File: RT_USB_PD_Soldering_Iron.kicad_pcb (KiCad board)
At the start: 4 copper layers, 75 x 11 mm, 63 parts, among them J1 USB_C_Receptacle_USB2.0, J2 35RASMT4BHNTRX, SW1 SW_Push, SW2 SW_Push, U1 SPX3819M5-L-3-3, U2 BMI270, U3 DRTR5V0U4S-7, U5 STM32G431Kxxx, U6 TPS25982ONRGET, U7 OPA376AIDCKR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

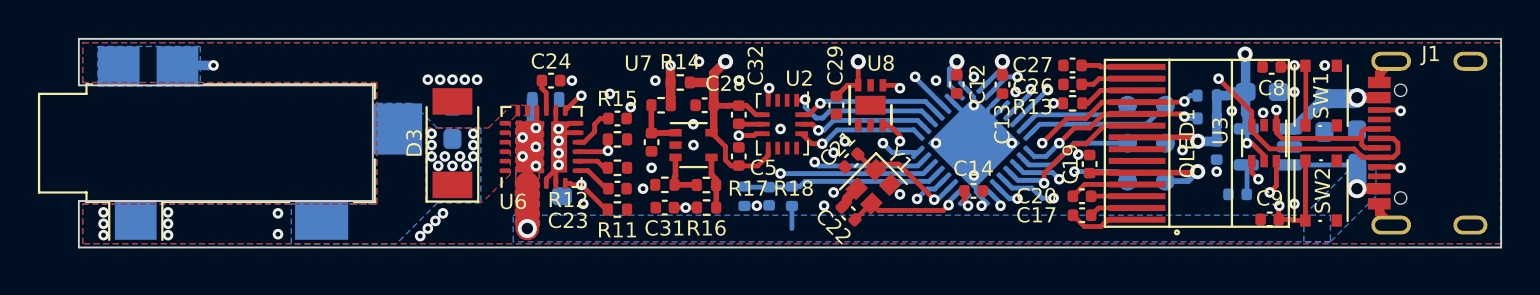
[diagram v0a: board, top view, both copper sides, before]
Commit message: update libs/parts
update 0402 footprints for silkscreen
move volate/tolerance to value
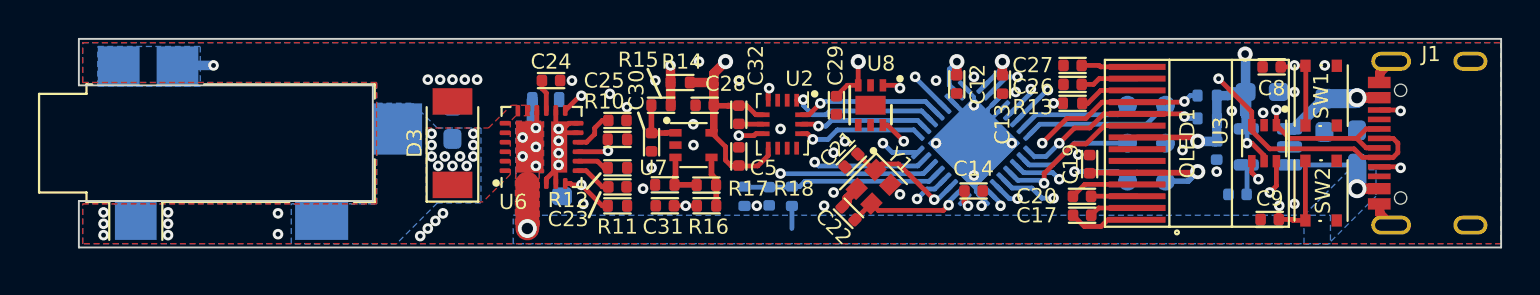
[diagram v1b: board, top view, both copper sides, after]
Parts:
- C1, C15, C16, C2, C33: value 10uF -> 10uF 35v
- C12, C13, C14, C18, C19, C28, C29, C32, C5, C8, C9: value 0.1uF -> 0.1uF 50v; footprint Capacitor_SMD:C_0402_1005Metric -> Basic_SMD:C_0402_1005Metric
- C17, C20, C4: value 1u -> 1u 50v; footprint Capacitor_SMD:C_0402_1005Metric -> Basic_SMD:C_0402_1005Metric
- C21, C22: value 6.8p -> 6.8p 50v; footprint Capacitor_SMD:C_0402_1005Metric -> Basic_SMD:C_0402_1005Metric
- C23, C25, C3, C30, C31: value 10000pF -> 10000pF 50v; footprint Capacitor_SMD:C_0402_1005Metric -> Basic_SMD:C_0402_1005Metric
- C24: value 1200pF -> 1200pF 50v; footprint Capacitor_SMD:C_0402_1005Metric -> Basic_SMD:C_0402_1005Metric
- C26, C27: value 2.2u -> 2.2u 25v; footprint Capacitor_SMD:C_0402_1005Metric -> Basic_SMD:C_0402_1005Metric
- J1: value USB_C_Receptacle_USB2.0 -> USB4105-GF-A
- R10: value 1870 -> 1870 0.5%; footprint Resistor_SMD:R_0402_1005Metric -> Basic_SMD:R_0402_1005Metric
- R11: value 10K -> 10K 5%; footprint Resistor_SMD:R_0402_1005Metric -> Basic_SMD:R_0402_1005Metric
- R12: value 220 -> 220 1%; footprint Resistor_SMD:R_0402_1005Metric -> Basic_SMD:R_0402_1005Metric
- R13: value 390K -> 390K 5%; footprint Resistor_SMD:R_0402_1005Metric -> Basic_SMD:R_0402_1005Metric
- R14: value 1M -> 1M 5%; footprint Resistor_SMD:R_0402_1005Metric -> Basic_SMD:R_0402_1005Metric
- R15: value 5.6K -> 5.6K 5%; footprint Resistor_SMD:R_0402_1005Metric -> Basic_SMD:R_0402_1005Metric
- R16, R6, R7: value 2.2K -> 2.2K 5%; footprint Resistor_SMD:R_0402_1005Metric -> Basic_SMD:R_0402_1005Metric
- R17: value 560 -> 560 0.1%; footprint Resistor_SMD:R_0402_1005Metric -> Basic_SMD:R_0402_1005Metric
- R18: value 100K -> 100K 0.1%; footprint Resistor_SMD:R_0402_1005Metric -> Basic_SMD:R_0402_1005Metric
- R2: value 12K -> 12K 1%; footprint Resistor_SMD:R_0402_1005Metric -> Basic_SMD:R_0402_1005Metric
- R4: value 1.8K -> 1.8K 1%; footprint Resistor_SMD:R_0402_1005Metric -> Basic_SMD:R_0402_1005Metric
- moved R11 0.20 mm to (128.4, 128.3)
- moved C25 0.10 mm to (128.4, 123.8)
- moved C31 0.10 mm to (130.9, 128.3)
- moved R16 0.10 mm to (133.1, 128.3)
- moved C23 0.09 mm to (128.4, 127.3)

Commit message: Minor changes
moved oled connector slightly. Moved I2C pullup resistors
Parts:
- R6, R7: moved to F.Cu
- moved R7 15.6 mm to (144.0, 124.0)
- moved R6 15.5 mm to (144.0, 122.9)
- moved C2 4.03 mm to (159.6, 125.2), turned to -90 degrees
- moved C18 1.81 mm to (158.2, 125.2)
- moved TP1 1.30 mm to (154.0, 127.0)
- moved TP2 1.30 mm to (154.0, 123.0)
- moved TP3 1.30 mm to (156.0, 123.0)
- moved TP4 1.30 mm to (154.0, 125.0)
- moved TP5 1.30 mm to (156.0, 127.0)
- moved TP6 1.30 mm to (156.0, 125.0)
- moved C3 0.75 mm to (160.4, 127.5)
- moved C13 0.31 mm to (148.4, 121.9)
- moved OLED1 0.31 mm to (155.5, 125.0)
- moved C17 0.30 mm to (152.6, 128.8)
- moved C19 0.30 mm to (153.0, 126.1)
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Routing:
- net +3V3: track 80.9 -> 77.6 mm, vias 9 -> 11
- net /I2C1_SDA: track 23.3 -> 20.4 mm, vias 4 -> 3
- net /I2C1_SCL: track 20.2 -> 17.9 mm, vias 3 -> 2
- net /SWO: track 6.10 -> 4.80 mm
- net /SWDIO: track 5.97 -> 4.67 mm
- net /SWCLK: track 7.77 -> 6.47 mm
- net /NRST: track 14.1 -> 12.9 mm
- net /USB_DM: track 25.3 -> 24.7 mm
- net /DISP_RST#: track 8.50 -> 8.08 mm, vias 1 -> 2
- net GND: vias 56 -> 57

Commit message: minor layout changes
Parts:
- moved R14 1.40 mm to (133.1, 122.0)
- moved R15 0.78 mm to (131.3, 122.5), turned to -90 degrees
- moved C28 0.10 mm to (133.1, 123.0)
- moved C30 0.10 mm to (130.3, 125.0)
- moved C2 0.10 mm to (159.6, 125.1)
- moved C32 0.10 mm to (134.9, 123.5)
- moved C5 0.10 mm to (134.9, 125.7)
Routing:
- net +3V3: track 77.6 -> 76.1 mm

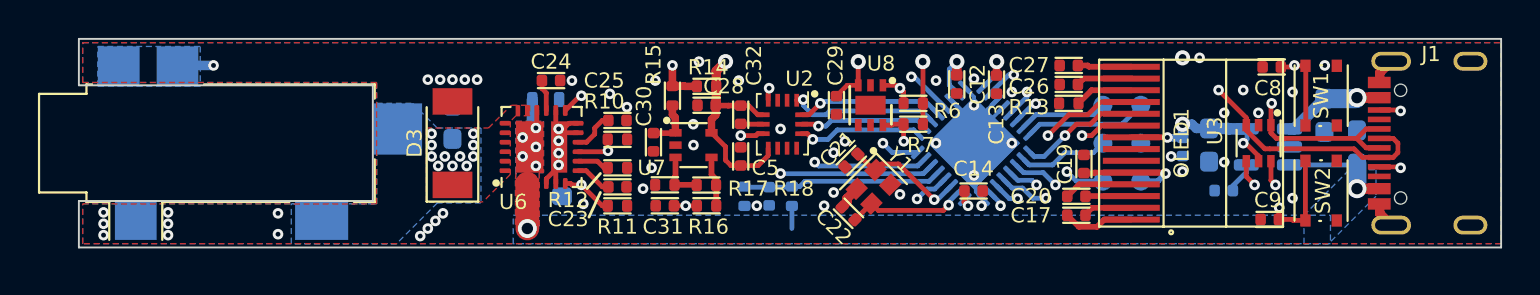
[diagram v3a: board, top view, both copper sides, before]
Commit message: redo USB traces with impedence calculations
rename usb traces and do calculations for 90 ohm impedence
also change voltage sense resistors to higher values
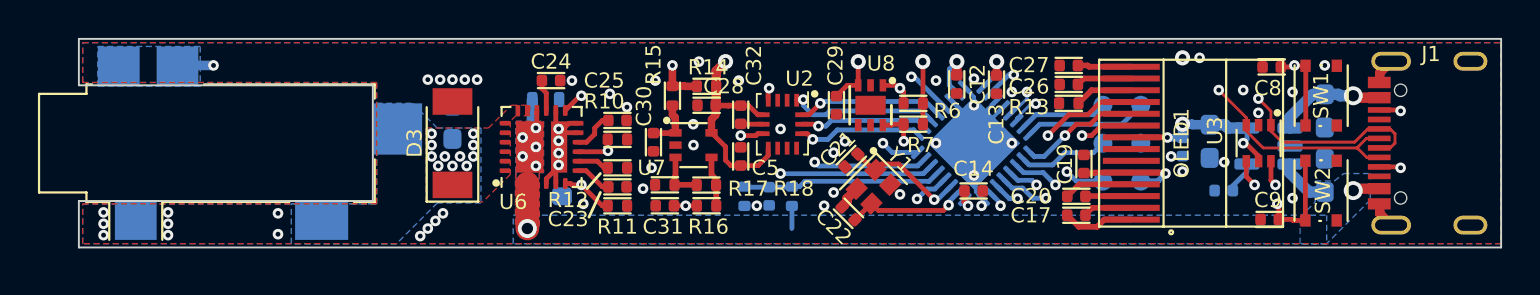
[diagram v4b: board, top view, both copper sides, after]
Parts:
- moved C1 2.27 mm to (165.7, 126.7)
- moved C33 0.23 mm to (165.7, 123.3)
- moved C2 0.20 mm to (159.6, 124.9)
- moved U1 0.05 mm to (162.7, 125.2)
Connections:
- net /USB_DM renamed /USB_N
- net /USB_DP renamed /USB_P
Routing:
- net IN: track 22.4 -> 21.1 mm
- net /USB_N: track 24.7 -> 23.6 mm
- net /USB_P: track 23.0 -> 23.9 mm
- net GND: vias 57 -> 56

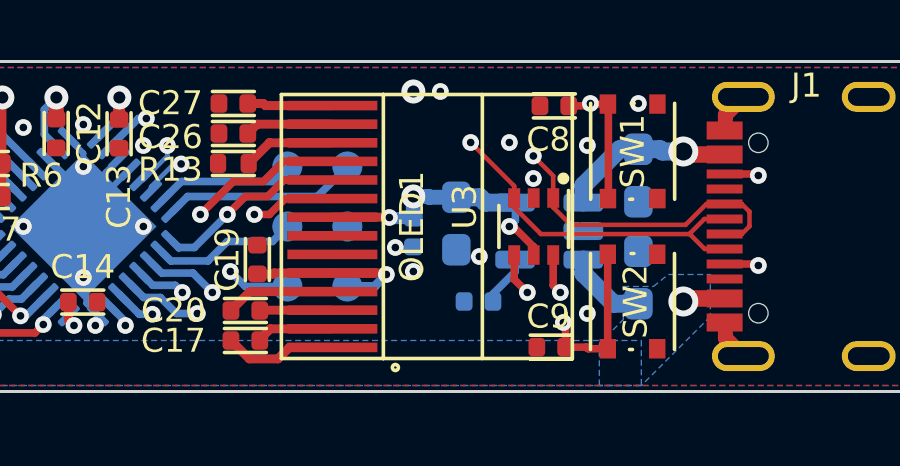
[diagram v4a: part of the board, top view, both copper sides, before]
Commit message: complete ground path for usb
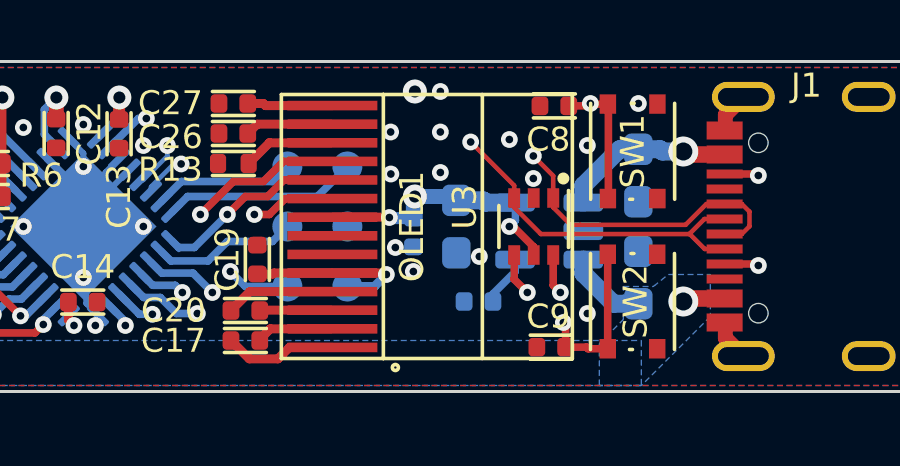
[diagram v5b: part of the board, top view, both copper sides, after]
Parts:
- moved C2 0.10 mm to (159.6, 125.0)
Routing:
- net /BTN2: track 21.2 -> 35.9 mm
- net GND: vias 56 -> 60

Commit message: more usb improvements
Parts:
- moved C2 0.11 mm to (159.6, 125.1)
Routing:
- net /CC2: track 24.8 -> 25.9 mm
